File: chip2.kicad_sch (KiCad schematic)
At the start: 54 parts, among them J1 Conn_01x04, J3 Conn_01x02, J4 USB_C_Receptacle_USB2.0, J5 EXP, J6 EXP, Q1 AO3400A, Q2 UMH3N, SW1 TS-1102S-C-A-B, SW2 TS-1102S-C-A-B, U1 ESP32-PICO-D4, U2 MT3420C, U3 CP2104

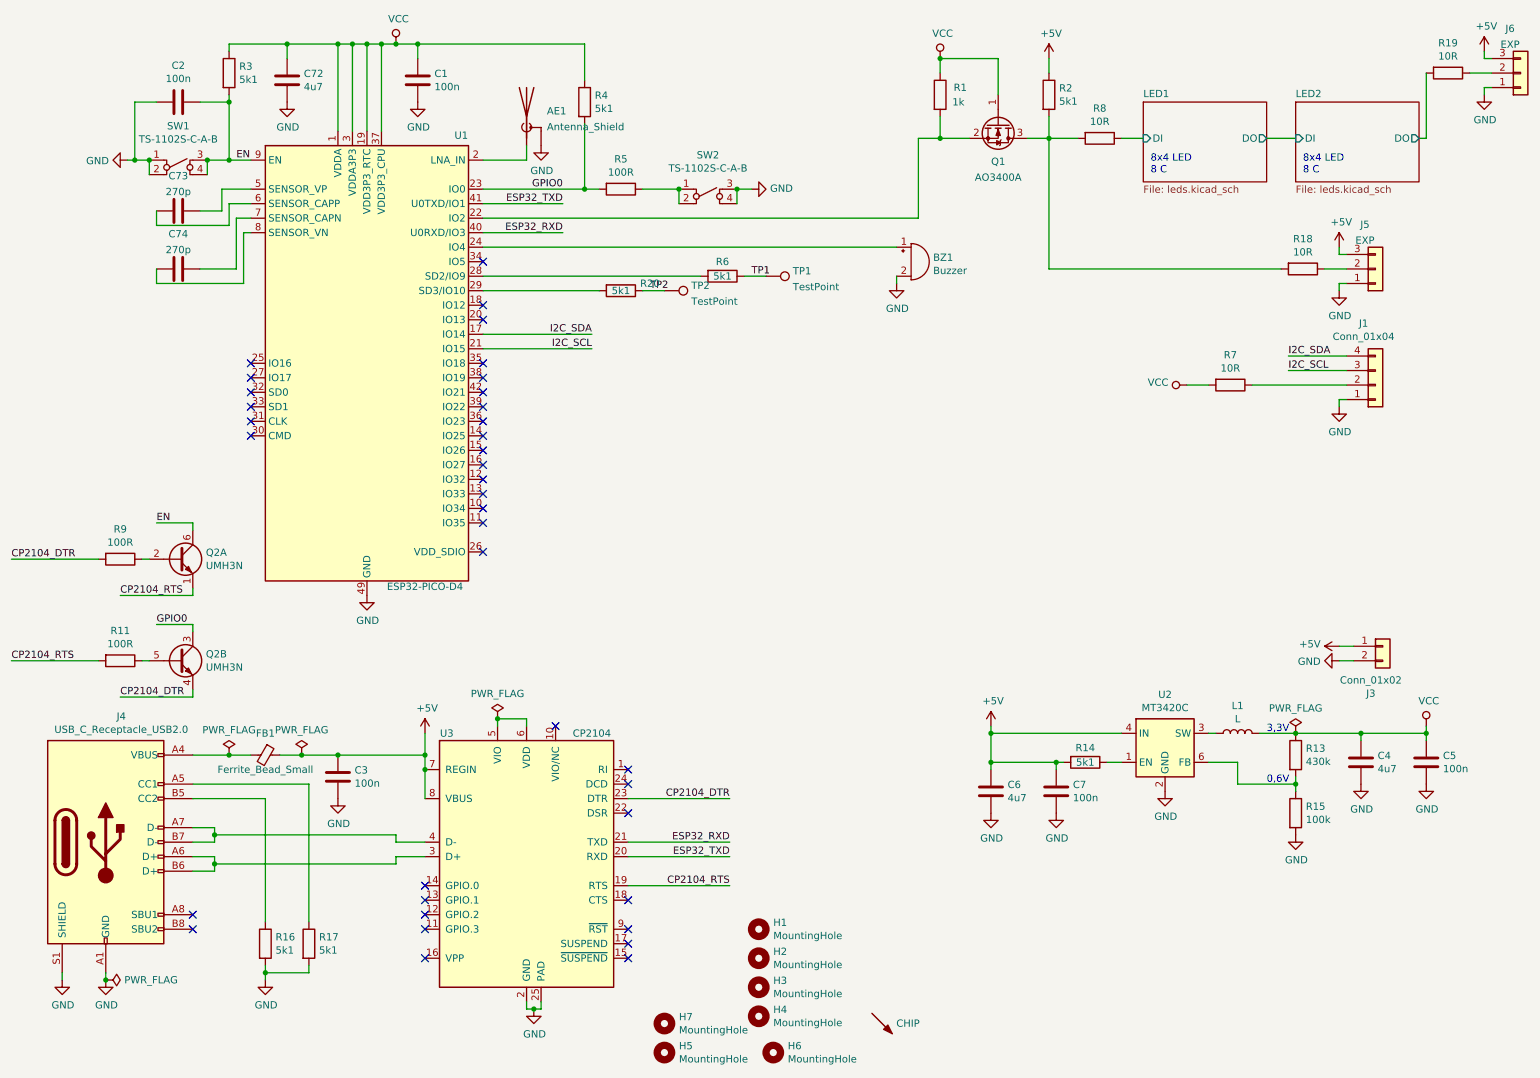
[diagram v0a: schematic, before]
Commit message: Changed resistor values for level shifter
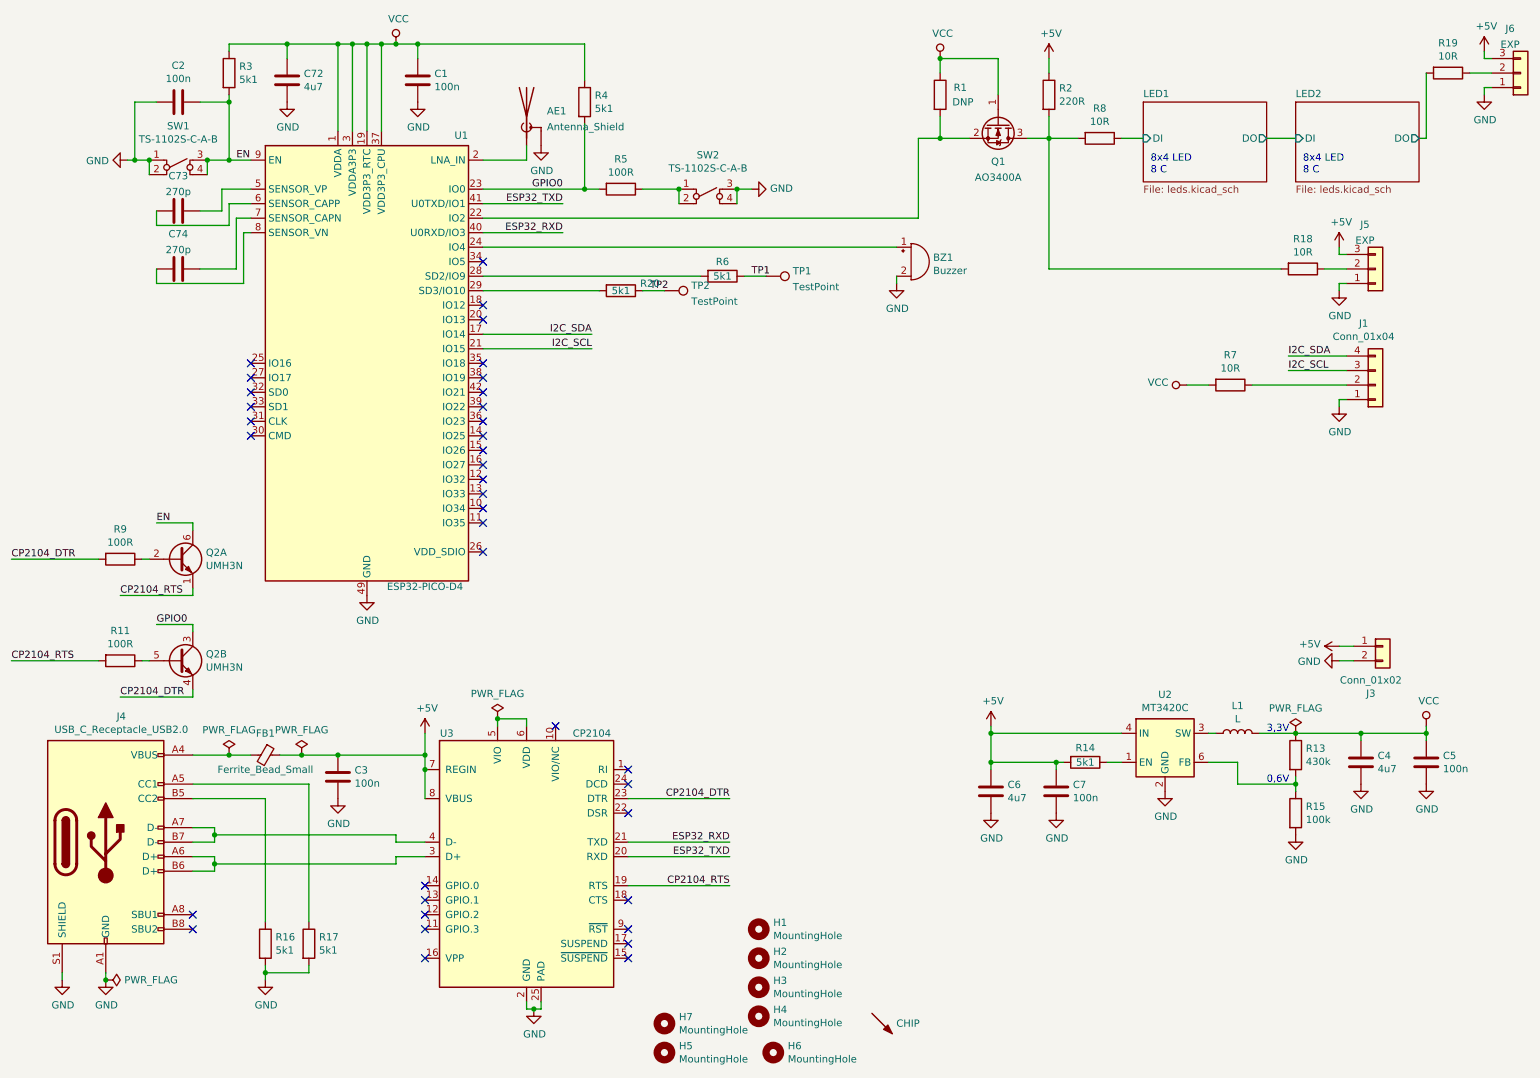
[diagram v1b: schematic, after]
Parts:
- R1: value 1k -> DNP; LCSC Part C21190 -> (none)
- R2: value 5k1 -> 220R; LCSC Part C269716 -> (none)
- U2: LCSC Part C62892 -> C88169
